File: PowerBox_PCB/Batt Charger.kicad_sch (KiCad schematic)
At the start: 20 parts, among them U10 BQ25887RGER

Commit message: Finished
Basically done
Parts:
- added TP11: (no value), Custom_Footprints:PAD-2x2, symbol Custom_Symbols:Pad-2x2
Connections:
- net VOUT: now also TP11.1 (PAD)
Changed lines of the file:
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@@
+		)
+	)
+	(label "VOUT"
+		(at 195.58 50.8 180)
+		(effects
+			(font
+				(size 1.27 1.27)
+			)
+			(justify right bottom)
 		)
 	)
@@
 					(unit 1)
 				)
+			)
+		)
+	)
+	(symbol
+		(lib_id "Custom_Symbols:Pad-2x2")
+		(at 198.12 50.8 90)
+		(unit 1)
+		(body_style 1)
+		(exclude_from_sim no)
+		(in_bom yes)
+		(on_board yes)
+		(in_pos_files yes)
+		(dnp no)
+		(fields_autoplaced yes)
+		(property "Reference" "TP11"
+			(at 199.39 50.7999 90)
+			(show_name no)
+			(do_not_autoplace no)
+			(effects
+				(font
+					(size 1.27 1.27)
+				)
+				(justify right)
+			)
+		)
+		(property "Value" ""
+			(at 198.12 50.8 0)
+			(show_name no)
+			(do_not_autoplace no)
+			(effects
+				(font
+					(size 1.27 1.27)
+				)
+			)
+		)
+		(property "Footprint" "Custom_Footprints:PAD-2x2"
+			(at 198.12 50.8 0)
+			(hide yes)
+			(show_name no)
+			(do_not_autoplace no)
+			(effects
+				(font
+					(size 1.27 1.27)
+				)
+			)
+		)
+		(property "Datasheet" ""
+			(at 198.12 50.8 0)
+			(hide yes)
+			(show_name no)
+			(do_not_autoplace no)
+			(effects
+				(font
+					(size 1.27 1.27)
+				)
+			)
+		)
+		(property "Description" ""
+			(at 198.12 50.8 0)
+			(hide yes)
+			(show_name no)
+			(do_not_autoplace no)
+			(effects
+				(font
+					(size 1.27 1.27)
+				)
+			)
+		)
+		(pin "1"
+		)
+		(instances
+			(project "PowerBox_PCB"
+				(path "/b0254e12-8cc0-427f-8cea-8f6ec8f66525/da3152ce-e99b-41cb-8d30-a5dc30414d8e"
+					(reference "TP11")
+					(unit 1)
+				)

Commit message: .
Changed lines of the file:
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@@
+	(wire
+		(pts
+			(xy 179.07 97.79) (xy 175.26 97.79)
+		)
+		(stroke
+			(width 0)
+			(type default)
+		)
+	)
 	(wire
 		(pts
@@
 	(wire
 		(pts
-			(xy 109.22 66.04) (xy 109.22 59.69)
-		)
-		(stroke
-			(width 0)
-			(type default)
-		)
-	)
-	(wire
-		(pts
 			(xy 167.64 91.44) (xy 167.64 92.71)
 		)
@@
 	(wire
 		(pts
-			(xy 193.04 86.36) (xy 193.04 82.55)
+			(xy 194.31 86.36) (xy 194.31 82.55)
 		)
 		(stroke
@@
 	(wire
 		(pts
-			(xy 193.04 82.55) (xy 191.77 82.55)
+			(xy 194.31 82.55) (xy 191.77 82.55)
 		)
 		(stroke
@@
 	(wire
 		(pts
-			(xy 109.22 59.69) (xy 105.41 59.69)
+			(xy 109.22 66.04) (xy 104.14 66.04)
 		)
 		(stroke
@@
 	(symbol
 		(lib_id "power:GND")
-		(at 193.04 86.36 0)
+		(at 194.31 86.36 0)
 		(unit 1)
 		(body_style 1)
@@
 		(dnp no)
 		(property "Reference" "#PWR032"
-			(at 193.04 92.71 0)
+			(at 194.31 92.71 0)
 			(hide yes)
 			(show_name no)
@@
 		)
 		(property "Value" "GND"
-			(at 193.04 90.424 0)
+			(at 194.31 90.424 0)
 			(show_name no)
 			(do_not_autoplace no)
@@
 		)
 		(property "Footprint" ""
-			(at 193.04 86.36 0)
+			(at 194.31 86.36 0)
 			(hide yes)
 			(show_name no)
@@
 		)
 		(property "Datasheet" ""
-			(at 193.04 86.36 0)
+			(at 194.31 86.36 0)
 			(hide yes)
 			(show_name no)
@@
 		)
 		(property "Description" "Power symbol creates a global label with name \"GND\" , ground"
-			(at 193.04 86.36 0)
+			(at 194.31 86.36 0)
 			(hide yes)
 			(show_name no)
@@
 	(symbol
 		(lib_id "power:GND")
-		(at 105.41 59.69 0)
+		(at 104.14 66.04 0)
 		(unit 1)
 		(body_style 1)
@@
 		(dnp no)
 		(property "Reference" "#PWR042"
-			(at 105.41 66.04 0)
+			(at 104.14 72.39 0)
 			(hide yes)
 			(show_name no)
@@
 		)
 		(property "Value" "GND"
-			(at 105.41 63.754 0)
+			(at 104.14 70.104 0)
 			(show_name no)
 			(do_not_autoplace no)
@@
 		)
 		(property "Footprint" ""
-			(at 105.41 59.69 0)
+			(at 104.14 66.04 0)
 			(hide yes)
 			(show_name no)
@@
 		)
 		(property "Datasheet" ""
-			(at 105.41 59.69 0)
+			(at 104.14 66.04 0)
 			(hide yes)
 			(show_name no)
@@
 		)
 		(property "Description" "Power symbol creates a global label with name \"GND\" , ground"
-			(at 105.41 59.69 0)
+			(at 104.14 66.04 0)
 			(hide yes)
 			(show_name no)
@@
 		(in_pos_files yes)
 		(dnp no)
-		(fields_autoplaced yes)
 		(property "Reference" "C29"
-			(at 171.45 90.17 90)
+			(at 176.53 96.52 90)
 			(show_name no)
 			(do_not_autoplace no)
@@
 		)
 		(property "Value" "44uF"
-			(at 171.45 92.71 90)
+			(at 175.26 99.06 90)
 			(show_name no)
 			(do_not_autoplace no)
@@
 		(in_pos_files yes)
 		(dnp no)
-		(fields_autoplaced yes)
 		(property "Reference" "R33"
-			(at 116.84 68.5799 0)
+			(at 114.3 59.944 90)
 			(show_name no)
 			(do_not_autoplace no)
@@
 		)
 		(property "Value" "10kΩ"
-			(at 116.84 71.1199 0)
+			(at 114.3 65.532 90)
 			(show_name no)
 			(do_not_autoplace no)
@@
 		(in_pos_files yes)
 		(dnp no)
-		(fields_autoplaced yes)
 		(property "Reference" "R34"
-			(at 119.38 68.5799 0)
+			(at 116.84 59.944 90)
 			(show_name no)
 			(do_not_autoplace no)
@@
 		)
 		(property "Value" "10kΩ"
-			(at 119.38 71.1199 0)
+			(at 116.84 65.532 90)
 			(show_name no)
 			(do_not_autoplace no)
@@
 		(in_pos_files yes)
 		(dnp no)
-		(fields_autoplaced yes)
 		(property "Reference" "R31"
-			(at 111.76 68.5799 0)
+			(at 109.22 59.944 90)
 			(show_name no)
 			(do_not_autoplace no)
@@
 		)
 		(property "Value" "10kΩ"
-			(at 111.76 71.1199 0)
+			(at 109.22 65.532 90)
 			(show_name no)
 			(do_not_autoplace no)
@@
 		(dnp no)
 		(property "Reference" "R39"
-			(at 113.03 102.87 90)
+			(at 113.03 96.52 90)
 			(show_name no)
 			(do_not_autoplace no)
@@
 		)
 		(property "Value" "10Ω_2W"
-			(at 113.03 100.33 90)
+			(at 105.664 96.774 90)
 			(show_name no)
 			(do_not_autoplace no)
@@
 		(lib_id "Custom_Symbols:5.23kRes")
 		(at 107.95 102.87 0)
-		(unit 1)
-		(body_style 1)
-		(exclude_from_sim no)
-		(in_bom yes)
-		(on_board yes)
-		(in_pos_files yes)
-		(dnp no)
-		(fields_autoplaced yes)
+		(mirror y)
+		(unit 1)
+		(body_style 1)
+		(exclude_from_sim no)
+		(in_bom yes)
+		(on_board yes)
+		(in_pos_files yes)
+		(dnp no)
 		(property "Reference" "R36"
-			(at 110.49 101.5999 0)
+			(at 105.156 101.092 0)
 			(show_name no)
 			(do_not_autoplace no)
@@
 		)
 		(property "Value" "5.23kΩ"
-			(at 110.49 104.1399 0)
+			(at 105.156 103.632 0)
 			(show_name no)
 			(do_not_autoplace no)
@@
 		(in_pos_files yes)
 		(dnp no)
-		(fields_autoplaced yes)
 		(property "Reference" "R32"
-			(at 114.3 68.5799 0)
+			(at 111.76 59.944 90)
 			(show_name no)
 			(do_not_autoplace no)
@@
 		)
 		(property "Value" "10kΩ"
-			(at 114.3 71.1199 0)
+			(at 111.76 65.532 90)
 			(show_name no)
 			(do_not_autoplace no)
@@
 		(dnp no)
 		(property "Reference" "C27"
-			(at 187.96 90.17 90)
+			(at 193.04 81.534 90)
 			(show_name no)
 			(do_not_autoplace no)
@@
 		)
 		(property "Value" "10uf"
-			(at 187.96 87.63 90)
+			(at 191.262 83.82 90)
 			(show_name no)
 			(do_not_autoplace no)
@@
 	(symbol
 		(lib_id "power:GND")
-		(at 175.26 97.79 0)
+		(at 179.07 97.79 0)
 		(unit 1)
 		(body_style 1)
@@
 		(dnp no)
 		(property "Reference" "#PWR037"
-			(at 175.26 104.14 0)
+			(at 179.07 104.14 0)
 			(hide yes)
 			(show_name no)
@@
 		)
 		(property "Value" "GND"
-			(at 175.26 101.854 0)
+			(at 179.07 101.854 0)
 			(show_name no)
 			(do_not_autoplace no)
@@
 		)
 		(property "Footprint" ""
-			(at 175.26 97.79 0)
+			(at 179.07 97.79 0)
 			(hide yes)
 			(show_name no)
@@
 		)
 		(property "Datasheet" ""
-			(at 175.26 97.79 0)
+			(at 179.07 97.79 0)
 			(hide yes)
 			(show_name no)
@@
 		)
 		(property "Description" "Power symbol creates a global label with name \"GND\" , ground"
-			(at 175.26 97.79 0)
+			(at 179.07 97.79 0)
 			(hide yes)
 			(show_name no)
@@
 		(in_pos_files yes)
 		(dnp no)
-		(fields_autoplaced yes)
 		(property "Reference" "R40"
-			(at 113.03 87.63 90)
+			(at 113.03 93.98 90)
 			(show_name no)
 			(do_not_autoplace no)
@@
 		)
 		(property "Value" "300Ω"
-			(at 113.03 90.17 90)
+			(at 106.172 93.472 90)
 			(show_name no)
 			(do_not_autoplace no)
@@
 		(lib_id "Custom_Symbols:47nF_Cap")
 		(at 127 105.41 0)
+		(mirror y)
 		(unit 1)
 		(body_style 1)
@@
 		(dnp no)
 		(property "Reference" "C28"
-			(at 130.81 105.4099 0)
+			(at 123.444 104.394 0)
 			(show_name no)
 			(do_not_autoplace no)
@@
 		)
 		(property "Value" "47nF"
-			(at 132.842 107.696 0)
+			(at 121.412 106.6801 0)
 			(show_name no)
 			(do_not_autoplace no)
@@
 		)
 		(property "Footprint" "Capacitor_SMD:C_0805_2012Metric_Pad1.18x1.45mm_HandSolder"
-			(at 127.254 105.41 0)
+			(at 126.746 105.41 0)
 			(hide yes)
 			(show_name no)
@@
 		(in_pos_files yes)
 		(dnp no)
-		(fields_autoplaced yes)
 		(property "Reference" "R41"
-			(at 104.14 69.85 90)
+			(at 104.14 76.2 90)
 			(show_name no)
 			(do_not_autoplace no)
@@
 		)
 		(property "Value" "2.2kΩ"
-			(at 104.14 72.39 90)
+			(at 104.14 78.74 90)
 			(show_name no)
 			(do_not_autoplace no)
@@
 		(in_pos_files yes)
 		(dnp no)
-		(fields_autoplaced yes)
 		(property "Reference" "L4"
-			(at 98.1075 68.58 0)
+			(at 96.774 73.66 0)
 			(show_name no)
 			(do_not_autoplace no)
@@
 		)
 		(property "Value" "LED"
-			(at 98.1075 71.12 0)
-			(show_name no)
-			(do_not_autoplace no)
+			(at 97.536 78.994 0)
+			(show_name no)
+			(do_not_autoplace no)

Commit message: fix bom
bom
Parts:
- U18: value (none) -> LM1084RS-5.0
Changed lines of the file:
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@@
 		(in_pos_files yes)
 		(dnp no)
-		(fields_autoplaced yes)
 		(property "Reference" "U18"
 			(at 196.85 72.39 0)
@@
 			)
 		)
-		(property "Value" ""
-			(at 196.85 77.47 0)
+		(property "Value" "LM1084RS-5.0"
+			(at 196.85 70.358 0)
 			(show_name no)
 			(do_not_autoplace no)

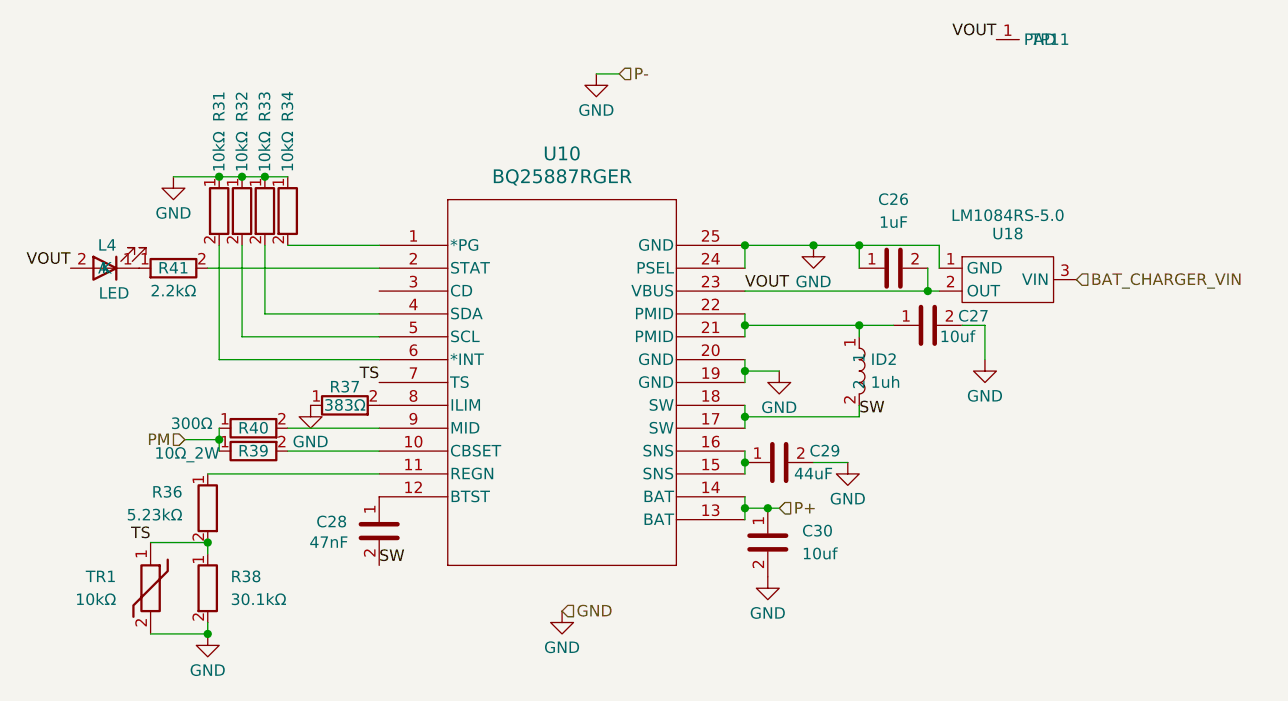
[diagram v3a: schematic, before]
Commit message: Changed HUSB238 to CH221K
HUSB238 Went out of stock so changed to CH221K
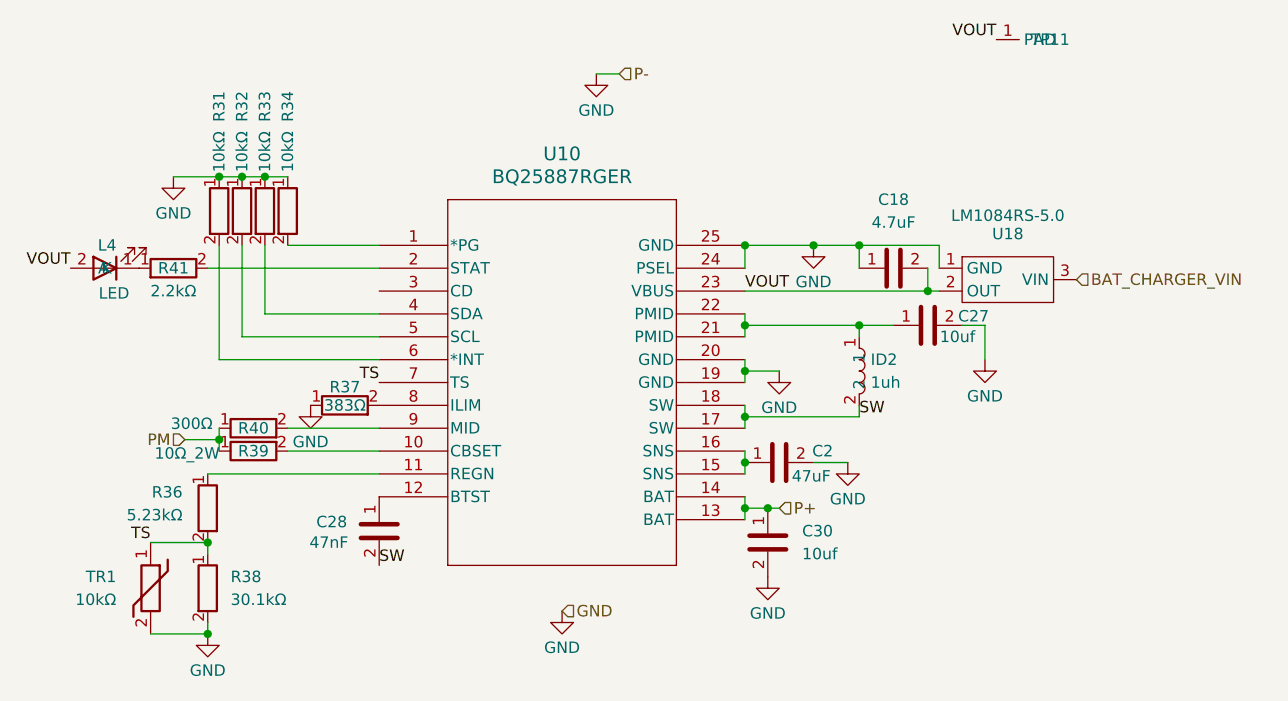
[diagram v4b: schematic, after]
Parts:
- removed C26: 1uF, Capacitor_SMD:C_0805_2012Metric_Pad1.18x1.45mm_HandSolder, symbol Custom_Symbols:1uF_Cap
- removed C29: 44uF, Capacitor_SMD:C_0805_2012Metric_Pad1.18x1.45mm_HandSolder, symbol Custom_Symbols:44uF_Cap
- added C18: 4.7uF, Capacitor_SMD:C_0805_2012Metric_Pad1.18x1.45mm_HandSolder, symbol Custom_Symbols:4.7uF_Cap
- added C2: 47uF, Capacitor_SMD:C_1210_3225Metric_Pad1.33x2.70mm_HandSolder, symbol Buck_TPS54620:47uF_Cap_1210
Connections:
- net GND: now also C18.1, C2.2
- net VOUT: now also C18.2
- net at U10.15 (SNS), U10.16 (SNS): now also C2.1
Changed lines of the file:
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@@
+	)
+	(junction
+		(at 167.64 97.79)
+		(diameter 0)
+		(color 0 0 0 0)
 	)
 	(junction
@@
 	)
 	(junction
-		(at 167.64 97.79)
-		(diameter 0)
-		(color 0 0 0 0)
-	)
-	(junction
 		(at 114.3 66.04)
 		(diameter 0)
@@
 	(wire
 		(pts
+			(xy 127 81.28) (xy 114.3 81.28)
+		)
+		(stroke
+			(width 0)
+			(type default)
+		)
+	)
+	(wire
+		(pts
+			(xy 167.64 76.2) (xy 167.64 73.66)
+		)
+		(stroke
+			(width 0)
+			(type default)
+		)
+	)
+	(wire
+		(pts
+			(xy 109.22 66.04) (xy 104.14 66.04)
+		)
+		(stroke
+			(width 0)
+			(type default)
+		)
+	)
+	(wire
+		(pts
+			(xy 116.84 93.98) (xy 127 93.98)
+		)
+		(stroke
+			(width 0)
+			(type default)
+		)
+	)
+	(wire
+		(pts
+			(xy 189.23 78.74) (xy 187.96 78.74)
+		)
+		(stroke
+			(width 0)
+			(type default)
+		)
+	)
+	(wire
+		(pts
+			(xy 167.64 87.63) (xy 171.45 87.63)
+		)
+		(stroke
+			(width 0)
+			(type default)
+		)
+	)
+	(wire
+		(pts
 			(xy 167.64 97.79) (xy 167.64 99.06)
-		)
-		(stroke
-			(width 0)
-			(type default)
-		)
-	)
-	(wire
-		(pts
-			(xy 127 81.28) (xy 114.3 81.28)
-		)
-		(stroke
-			(width 0)
-			(type default)
-		)
-	)
-	(wire
-		(pts
-			(xy 167.64 76.2) (xy 167.64 73.66)
-		)
-		(stroke
-			(width 0)
-			(type default)
-		)
-	)
-	(wire
-		(pts
-			(xy 109.22 66.04) (xy 104.14 66.04)
-		)
-		(stroke
-			(width 0)
-			(type default)
-		)
-	)
-	(wire
-		(pts
-			(xy 116.84 93.98) (xy 127 93.98)
-		)
-		(stroke
-			(width 0)
-			(type default)
-		)
-	)
-	(wire
-		(pts
-			(xy 189.23 78.74) (xy 187.96 78.74)
-		)
-		(stroke
-			(width 0)
-			(type default)
-		)
-	)
-	(wire
-		(pts
-			(xy 167.64 87.63) (xy 171.45 87.63)
 		)
 		(stroke
@@
 	)
 	(symbol
-		(lib_id "Custom_Symbols:44uF_Cap")
-		(at 171.45 97.79 90)
-		(unit 1)
-		(body_style 1)
-		(exclude_from_sim no)
-		(in_bom yes)
-		(on_board yes)
-		(in_pos_files yes)
-		(dnp no)
-		(property "Reference" "C29"
-			(at 176.53 96.52 90)
-			(show_name no)
-			(do_not_autoplace no)
-			(effects
-				(font
-					(size 1.27 1.27)
-				)
-			)
-		)
-		(property "Value" "44uF"
-			(at 175.26 99.06 90)
-			(show_name no)
-			(do_not_autoplace no)
-			(effects
-				(font
-					(size 1.27 1.27)
-				)
-			)
-		)
-		(property "Footprint" "Capacitor_SMD:C_0805_2012Metric_Pad1.18x1.45mm_HandSolder"
-			(at 171.45 97.79 0)
-			(hide yes)
-			(show_name no)
-			(do_not_autoplace no)
-			(effects
-				(font
-					(size 1.27 1.27)
-				)
-			)
-		)
-		(property "Datasheet" ""
-			(at 171.45 97.79 0)
-			(hide yes)
-			(show_name no)
-			(do_not_autoplace no)
-			(effects
-				(font
-					(size 1.27 1.27)
-				)
-			)
-		)
-		(property "Description" ""
-			(at 171.45 97.79 0)
-			(hide yes)
-			(show_name no)
-			(do_not_autoplace no)
-			(effects
-				(font
-					(size 1.27 1.27)
-				)
-			)
-		)
-		(pin "2"
-		)
-		(pin "1"
-		)
-		(instances
-			(project "PowerBox_PCB"
-				(path "/b0254e12-8cc0-427f-8cea-8f6ec8f66525/da3152ce-e99b-41cb-8d30-a5dc30414d8e"
-					(reference "C29")
-					(unit 1)
-				)
-			)
-		)
-	)
-	(symbol
 		(lib_id "Custom_Symbols:10kRes")
 		(at 114.3 69.85 0)
@@
 	)
 	(symbol
-		(lib_id "Custom_Symbols:1uF_Cap")
-		(at 184.15 76.2 90)
-		(unit 1)
-		(body_style 1)
-		(exclude_from_sim no)
-		(in_bom yes)
-		(on_board yes)
-		(in_pos_files yes)
-		(dnp no)
-		(fields_autoplaced yes)
-		(property "Reference" "C26"
-			(at 184.15 68.58 90)
-			(show_name no)
-			(do_not_autoplace no)
-			(effects
-				(font
-					(size 1.27 1.27)
-				)
-			)
-		)
-		(property "Value" "1uF"
-			(at 184.15 71.12 90)
-			(show_name no)
-			(do_not_autoplace no)
-			(effects
-				(font
-					(size 1.27 1.27)
-				)
-			)
-		)
-		(property "Footprint" "Capacitor_SMD:C_0805_2012Metric_Pad1.18x1.45mm_HandSolder"
-			(at 184.15 76.2 0)
-			(hide yes)
-			(show_name no)
-			(do_not_autoplace no)
-			(effects
-				(font
-					(size 1.27 1.27)
-				)
-			)
-		)
-		(property "Datasheet" ""
-			(at 184.15 76.2 0)
-			(hide yes)
-			(show_name no)
-			(do_not_autoplace no)
-			(effects
-				(font
-					(size 1.27 1.27)
-				)
-			)
-		)
-		(property "Description" ""
-			(at 184.15 76.2 0)
-			(hide yes)
-			(show_name no)
-			(do_not_autoplace no)
-			(effects
-				(font
-					(size 1.27 1.27)
-				)
-			)
-		)
-		(pin "2"
-		)
-		(pin "1"
-		)
-		(instances
-			(project "PowerBox_PCB"
-				(path "/b0254e12-8cc0-427f-8cea-8f6ec8f66525/da3152ce-e99b-41cb-8d30-a5dc30414d8e"
-					(reference "C26")
-					(unit 1)
-				)
-			)
-		)
-	)
-	(symbol
 		(lib_id "Custom_Symbols:5.23kRes")
 		(at 107.95 102.87 0)
@@
 	)
 	(symbol
+		(lib_id "Custom_Symbols:4.7uF_Cap")
+		(at 184.15 76.2 90)
+		(unit 1)
+		(body_style 1)
+		(exclude_from_sim no)
+		(in_bom yes)
+		(on_board yes)
+		(in_pos_files yes)
+		(dnp no)
+		(fields_autoplaced yes)
+		(property "Reference" "C18"
+			(at 184.15 68.58 90)
+			(show_name no)
+			(do_not_autoplace no)
+			(effects
+				(font
+					(size 1.27 1.27)
+				)
+			)
+		)
+		(property "Value" "4.7uF"
+			(at 184.15 71.12 90)
+			(show_name no)
+			(do_not_autoplace no)
+			(effects
+				(font
+					(size 1.27 1.27)
+				)
+			)
+		)
+		(property "Footprint" "Capacitor_SMD:C_0805_2012Metric_Pad1.18x1.45mm_HandSolder"
+			(at 184.15 76.2 0)
+			(hide yes)
+			(show_name no)
+			(do_not_autoplace no)
+			(effects
+				(font
+					(size 1.27 1.27)
+				)
+			)
+		)
+		(property "Datasheet" ""
+			(at 184.15 76.2 0)
+			(hide yes)
+			(show_name no)
+			(do_not_autoplace no)
+			(effects
+				(font
+					(size 1.27 1.27)
+				)
+			)
+		)
+		(property "Description" ""
+			(at 184.15 76.2 0)
+			(hide yes)
+			(show_name no)
+			(do_not_autoplace no)
+			(effects
+				(font
+					(size 1.27 1.27)
+				)
+			)
+		)
+		(pin "2"
+		)
+		(pin "1"
+		)
+		(instances
+			(project "PowerBox_PCB"
+				(path "/b0254e12-8cc0-427f-8cea-8f6ec8f66525/da3152ce-e99b-41cb-8d30-a5dc30414d8e"
+					(reference "C18")
+					(unit 1)
+				)
+			)
+		)
+	)
+	(symbol
 		(lib_id "power:GND")
 		(at 119.38 91.44 0)
@@
 					(unit 1)
 				)
+			)
+		)
+	)
+	(symbol
+		(lib_id "Buck_TPS54620:47uF_Cap_1210")
+		(at 171.45 97.79 90)
+		(unit 1)
+		(body_style 1)
+		(exclude_from_sim no)
+		(in_bom yes)
+		(on_board yes)
+		(in_pos_files yes)
+		(dnp no)
+		(property "Reference" "C2"
+			(at 176.276 96.52 90)
+			(show_name no)
+			(do_not_autoplace no)
+			(effects
+				(font
+					(size 1.27 1.27)
+				)
+			)
+		)
+		(property "Value" "47uF"
+			(at 175.006 99.314 90)
+			(show_name no)
+			(do_not_autoplace no)
+			(effects
+				(font
+					(size 1.27 1.27)
+				)
+			)
+		)
+		(property "Footprint" "Capacitor_SMD:C_1210_3225Metric_Pad1.33x2.70mm_HandSolder"
+			(at 171.45 97.79 0)
+			(hide yes)
+			(show_name no)
+			(do_not_autoplace no)
+			(effects
+				(font
+					(size 1.27 1.27)
+				)
+			)
+		)
+		(property "Datasheet" ""
+			(at 171.45 97.79 0)
+			(hide yes)
+			(show_name no)
+			(do_not_autoplace no)
+			(effects
+				(font
+					(size 1.27 1.27)
+				)
+			)
+		)
+		(property "Description" ""
+			(at 171.45 97.79 0)
+			(hide yes)
+			(show_name no)
+			(do_not_autoplace no)
+			(effects
+				(font
+					(size 1.27 1.27)
+				)
+			)
+		)
+		(pin "1"
+		)
+		(pin "2"
+		)
+		(instances
+			(project "PowerBox_PCB"
+				(path "/b0254e12-8cc0-427f-8cea-8f6ec8f66525/da3152ce-e99b-41cb-8d30-a5dc30414d8e"
+					(reference "C2")
+					(unit 1)
+				)
